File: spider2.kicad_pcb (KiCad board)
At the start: 2 copper layers, 137 x 72.5 mm, 120 parts, among them J1 NRJ6HH, J10 PJ-320A, J11 PJ359, J12 PJ359, J13 PJ359, J14 PJ359, J15 PJ359, J16 PJ359, J19 PJ359, J2 NRJ6HH, J20 PJ359, J3 PJ359, J4 PJ359, J5 PJ359, J6 PJ-320A, J7 PJ359, J8 PJ359, J9 PJ359, P1 USB4085, Q1 AOI4286, Q2 BC547, Q3 BC547, SW2 200MDP1T2B2M2QE, SW3 200MDP1T2B2M2QE, SW4 200MDP3T1B1M6QE, U2 LM7805_TO220, U4 LM4562, U5 MAX4062, U6 MAX4062, U7 PAM8406D

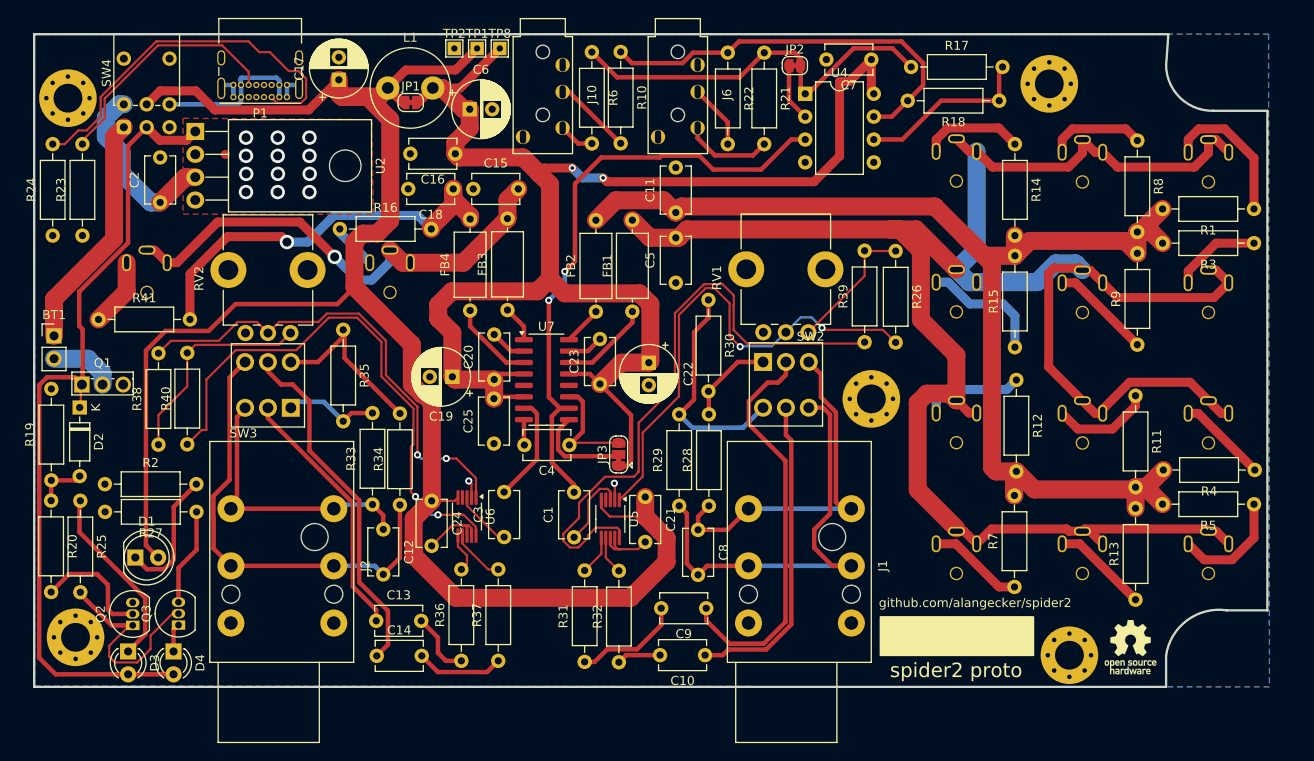
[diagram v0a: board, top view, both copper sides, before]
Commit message: 3.3V step down, fixed wrong CMV on balanced out, additional SMD footprints
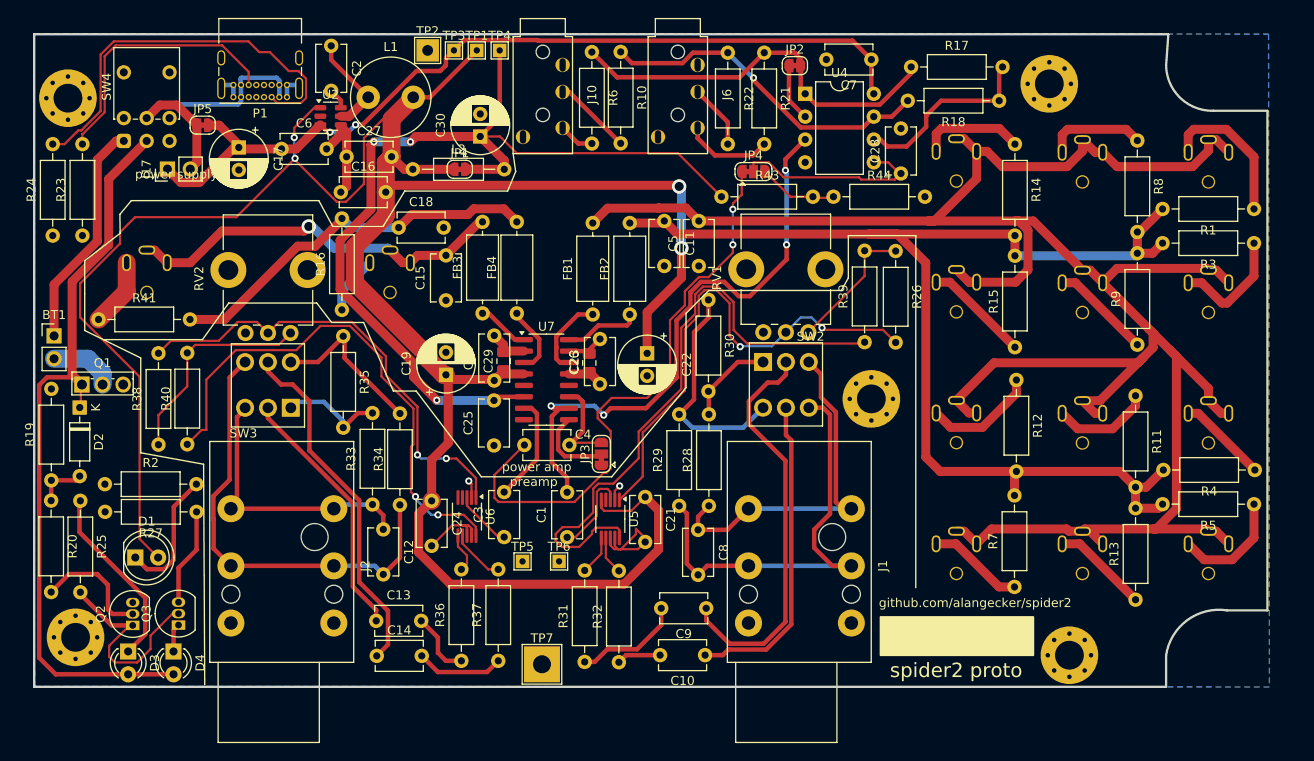
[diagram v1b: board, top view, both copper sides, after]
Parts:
- removed the REF** at (259.4, 98.7)
- removed TP8: 5VA, TestPoint:TestPoint_THTPad_1.5x1.5mm_Drill0.7mm
- added C26: alt, Capacitor_SMD:C_0805_2012Metric_Pad1.18x1.45mm_HandSolder, F.Cu at (199.3, 67.1)
- added C27: 22u, Capacitor_THT:C_Disc_D5.1mm_W3.2mm_P5.00mm, F.Cu at (172.3, 44.2)
- added C28: 100n, Capacitor_THT:C_Disc_D5.1mm_W3.2mm_P5.00mm, F.Cu at (233.9, 46.1)
- added C29: alt, Capacitor_SMD:C_0805_2012Metric_Pad1.18x1.45mm_HandSolder, F.Cu at (189.8, 66.9)
- added C30: NC, Capacitor_THT:CP_Radial_D6.3mm_P2.50mm, F.Cu at (187.2, 41.9)
- added J17: A, Connector_PinHeader_2.54mm:PinHeader_1x02_P2.54mm_Vertical, F.Cu at (152.4, 45.6)
- added JP4: SolderJumper_3_Bridged12, Jumper:SolderJumper-3_P1.3mm_Bridged12_RoundedPad1.0x1.5mm, F.Cu at (217.6, 45.8)
- added JP5: Jumper_2_Bridged, Jumper:SolderJumper-2_P1.3mm_Bridged_RoundedPad1.0x1.5mm, F.Cu at (156.4, 40.7)
- added L2: NC, Inductor_THT:L_Axial_L5.3mm_D2.2mm_P10.16mm_Horizontal_Vishay_IM-1, F.Cu at (179.7, 45.6)
- added R43: NC, Resistor_THT:R_Axial_DIN0207_L6.3mm_D2.5mm_P10.16mm_Horizontal, F.Cu at (214.0, 48.6)
- added R44: NC, Resistor_THT:R_Axial_DIN0207_L6.3mm_D2.5mm_P10.16mm_Horizontal, F.Cu at (226.4, 48.6)
- added TP3: V_in, TestPoint:TestPoint_THTPad_1.5x1.5mm_Drill0.7mm, F.Cu at (184.3, 32.4)
- added TP4: 3.3VA, TestPoint:TestPoint_THTPad_1.5x1.5mm_Drill0.7mm, F.Cu at (189.4, 32.4)
- added TP5: Floor, TestPoint:TestPoint_THTPad_1.5x1.5mm_Drill0.7mm, F.Cu at (191.9, 89.2)
- added TP6: Int., TestPoint:TestPoint_THTPad_1.5x1.5mm_Drill0.7mm, F.Cu at (196.0, 89.2)
- added TP7: GND, TestPoint:TestPoint_THTPad_4.0x4.0mm_Drill2.0mm, F.Cu at (194.1, 100.6)
- C1, C3: value 22u -> 470n
- C10, C13, C14, C9: value 22u -> 100n
- C6: value NC -> 22u; footprint Capacitor_THT:CP_Radial_D6.3mm_P2.50mm -> Capacitor_THT:C_Disc_D5.1mm_W3.2mm_P5.00mm
- C7: value NC -> 100n
- L1: value NC -> 4.7uH, >2A, <100mOhm
- R17, R18: value 10k -> 1k
- TP1: value 5V -> 3.3V
- TP2: footprint TestPoint:TestPoint_THTPad_1.5x1.5mm_Drill0.7mm -> TestPoint:TestPoint_THTPad_2.5x2.5mm_Drill1.2mm
- U2: value LM7805_TO220 -> AP63203WU; footprint Package_TO_SOT_THT:TO-220-4_Horizontal_TabDown -> Package_TO_SOT_SMD:TSOT-23-6
- U4: value LM4562 -> NE5532
- moved C2 25.8 mm to (170.6, 31.9), turned to -90 degrees
- moved C6 21.4 mm to (165.1, 43.3)
- moved U2 15.1 mm to (170.6, 39.7), turned to 0 degrees
- moved C16 13.4 mm to (171.7, 48.1), turned to 0 degrees
- moved C17 13.4 mm to (160.4, 43.2), turned to -90 degrees
- moved C15 12.7 mm to (183.4, 60.2), turned to 90 degrees
- moved JP1 9.21 mm to (184.9, 45.6)
- moved R16 8.99 mm to (171.8, 61.2), turned to 90 degrees
- moved C18 7.43 mm to (178.1, 52.1), turned to 0 degrees
- moved FB4 5.20 mm to (191.3, 61.6)
- moved FB1 4.42 mm to (199.7, 61.7)
- moved FB2 3.77 mm to (203.8, 61.7)
- moved C5 3.16 mm to (211.5, 56.3)
- moved TP2 2.97 mm to (181.4, 32.4)
- moved FB3 2.80 mm to (187.5, 61.6)
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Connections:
- net Net-(U7-VREF) renamed VREF
- C16 pad 1: +5VA -> GND
- C16 pad 2: GND -> +3.3V
- C17 pad 1: +5V -> VCC
- C19 pad 1: +5VA -> +3.3V
- C2 pad 1: Net-(SW4B-A) -> Net-(U2-SW)
- C2 pad 2: GND -> Net-(U2-BST)
- C20 pad 1: +5VA -> +3.3V
- C21 pad 1: +5V -> +3.3V
- C22 pad 1: +5VA -> +3.3V
- C23 pad 1: +5VA -> +3.3V
- C24 pad 1: +5V -> +3.3V
- C25 pad 2: +5VA -> +3.3VA
- C6 pad 1: +5VA -> VCC
- C7 pad 1: +5VA -> VCC
- D1 pad 2: +5V -> +3.3V
- D2 pad 1: V_BAT -> +BATT
- D3 pad 2: V_BAT -> +BATT
- D4 pad 2: V_BAT -> +BATT
- JP1 pad 1: +5V -> +3.3V
- JP1 pad 2: +5VA -> +3.3VA
- JP3 pad 1: +5VA -> +3.3V
- L1 pad 1: +5V -> Net-(U2-SW)
- L1 pad 2: +5VA -> +3.3V
- Q1 pad 1: V_BAT -> +BATT
- SW4 pad 2: V_BAT -> +BATT
- SW4 pad 4: Net-(SW4B-A) -> +BATT
- SW4 pad 5: +5V -> Net-(J17-Pin_2)
- TP1 pad 1: +5V -> +3.3V
- U2 pad 1: V_BAT -> +3.3V
- U2 pad 2: GND -> VCC
- U2 pad 3: Net-(SW4B-A) -> VCC
- U2 pad 4: (no net) -> GND
- U4 pad 5: GND -> Net-(JP4-C)
- U4 pad 8: +5VA -> VCC
- U5 pad 5: +5V -> +3.3V
- U6 pad 5: +5V -> +3.3V
- U7 pad 13: +5VA -> +3.3V
- U7 pad 4: +5VA -> +3.3V
- U7 pad 6: +5VA -> +3.3VA
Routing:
- net +3.3V: track 0.00 -> 276.4 mm, vias 0 -> 4
- net +5V: track 206.8 -> 0.00 mm
- net +5VA: track 174.0 -> 0.00 mm, vias 2 -> 0
- net +3.3VA: track 0.00 -> 105.7 mm, vias 0 -> 3
- net VCC: track 0.00 -> 96.0 mm, vias 0 -> 2
- net V_BAT: track 92.4 -> 0.00 mm
- net +BATT: track 0.00 -> 85.0 mm
- net VREF: track 2.84 -> 65.0 mm, vias 0 -> 2
- net Net-(JP4-C): track 0.00 -> 22.0 mm
- net Net-(SW4B-A): track 20.2 -> 0.00 mm
- net GND: track 45.1 -> 59.4 mm, vias 14 -> 2
- net Net-(J17-Pin_2): track 0.00 -> 12.2 mm
- net Net-(U2-SW): track 0.00 -> 11.3 mm
- net Net-(C15-Pad2): track 53.7 -> 43.1 mm
- net Net-(C5-Pad2): track 248.9 -> 258.1 mm
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- removed copper zone on F.Cu, net GND
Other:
- board text added: "power amp"
- board text added: "power supply"
- board text added: "preamp"

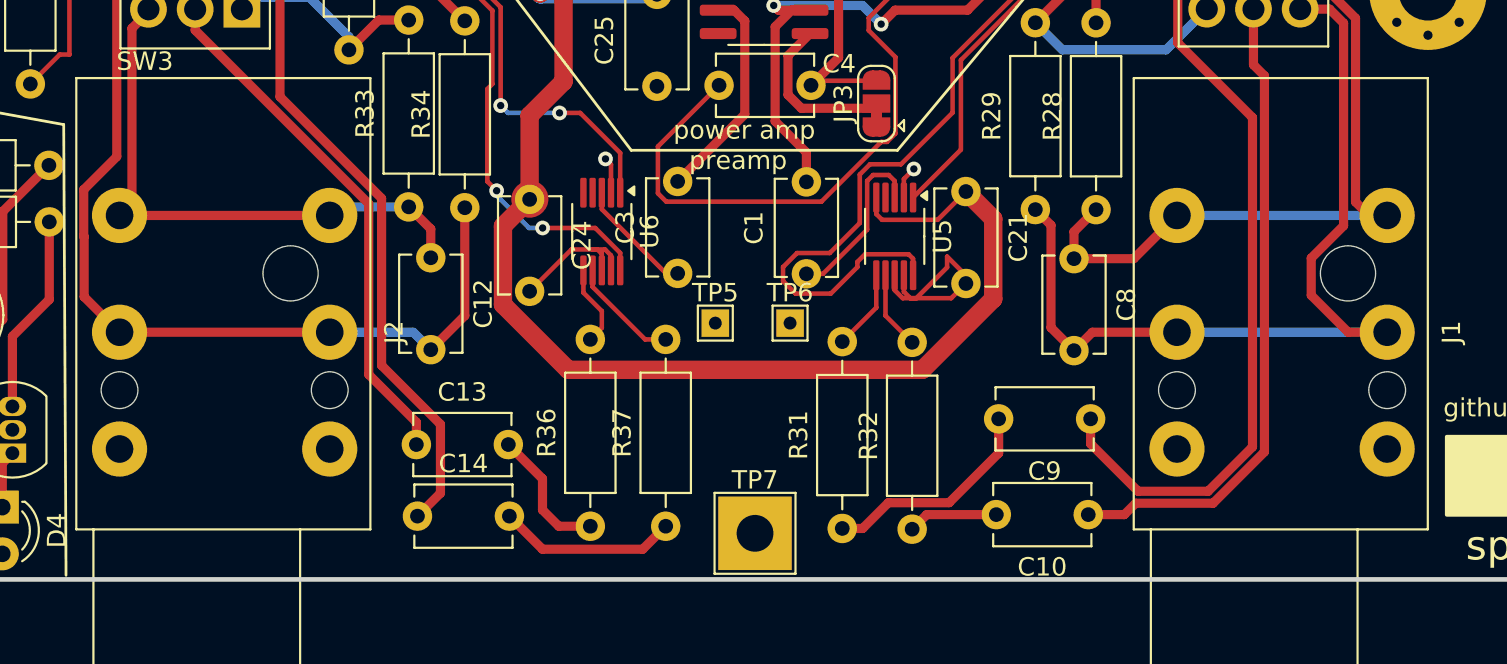
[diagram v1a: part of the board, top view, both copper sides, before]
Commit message: jumper for switching input jacks between GND and BIAS
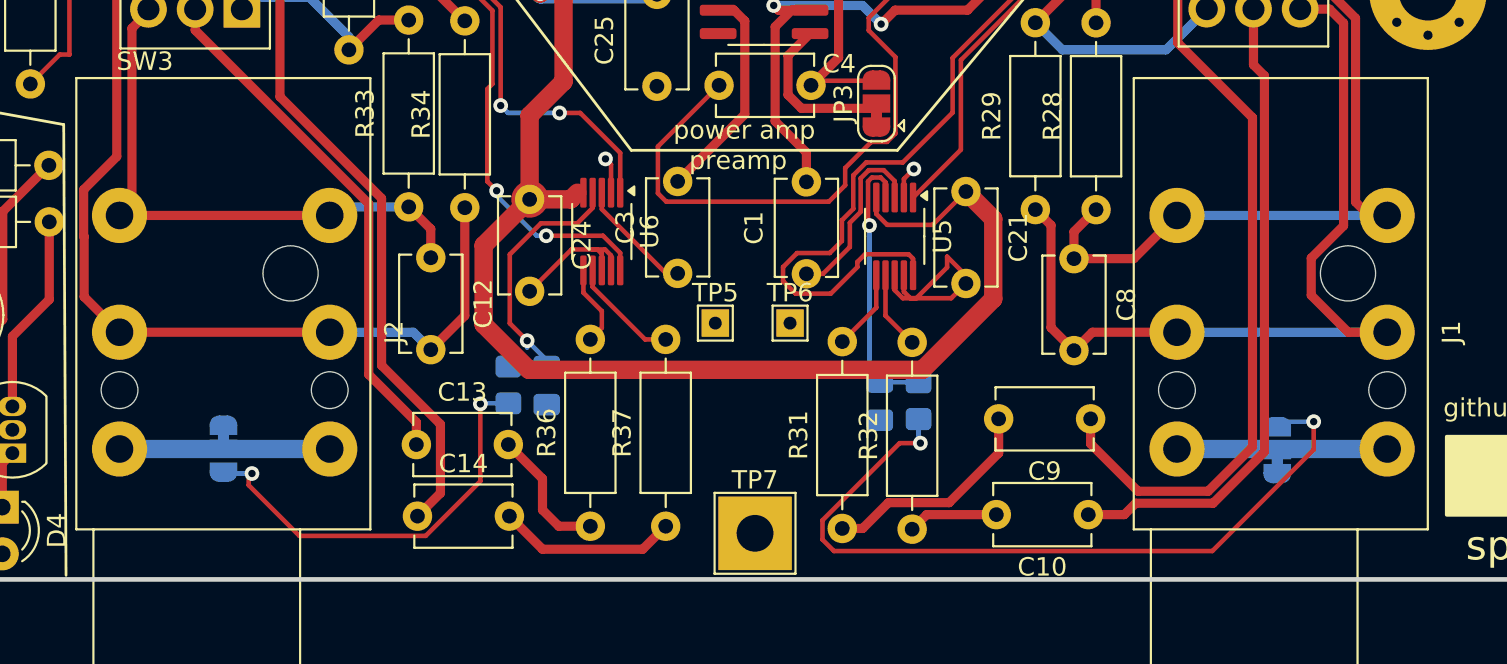
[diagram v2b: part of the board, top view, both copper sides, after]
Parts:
- added C31: NC, Capacitor_SMD:C_0805_2012Metric_Pad1.18x1.45mm_HandSolder, B.Cu at (200.8, 93.4)
- added C32: NC, Capacitor_SMD:C_0805_2012Metric_Pad1.18x1.45mm_HandSolder, B.Cu at (182.7, 92.6)
- added JP6: SolderJumper_3_Bridged12, Jumper:SolderJumper-3_P1.3mm_Bridged12_RoundedPad1.0x1.5mm, B.Cu at (222.5, 96.1)
- added JP7: SolderJumper_3_Bridged12, Jumper:SolderJumper-3_P1.3mm_Bridged12_RoundedPad1.0x1.5mm, B.Cu at (165.2, 96.0)
- added R42: NC, Resistor_SMD:R_0805_2012Metric_Pad1.20x1.40mm_HandSolder, B.Cu at (202.9, 93.4)
- added R45: NC, Resistor_SMD:R_0805_2012Metric_Pad1.20x1.40mm_HandSolder, B.Cu at (180.6, 92.5)
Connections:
- J1 pad S: GND -> Net-(JP6-C)
- J1 pad SN: GND -> Net-(JP6-C)
- J2 pad S: GND -> Net-(JP7-C)
- J2 pad SN: GND -> Net-(JP7-C)
- U5 pad 4: unconnected-(U5-BIAS-Pad4) -> Net-(U5-BIAS)
- U6 pad 4: unconnected-(U6-BIAS-Pad4) -> Net-(U6-BIAS)
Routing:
- net /Preamp Interpreter/BIAS: track 0.00 -> 42.3 mm, vias 0 -> 2
- net /Preamp Floor/BIAS: track 0.00 -> 23.0 mm, vias 0 -> 2
- net Net-(U6-BIAS): track 0.00 -> 15.8 mm, vias 0 -> 1
- net Net-(U5-BIAS): track 0.00 -> 15.3 mm, vias 0 -> 1
- net Net-(JP7-C): track 0.00 -> 11.4 mm
- net Net-(JP6-C): track 0.00 -> 11.4 mm
- net +3.3V: track 276.4 -> 281.5 mm
- net VREF: track 65.0 -> 65.6 mm
- net /Preamp Interpreter/OUT: track 9.61 -> 10.1 mm

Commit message: specify parts and load simulation R
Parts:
- added R46: NC, Resistor_THT:R_Axial_Power_L25.0mm_W9.0mm_P7.62mm_Vertical, F.Cu at (273.2, 66.2)
- FB1, FB2, FB3, FB4: value FerriteBead_Small -> 3A, >100 Ohm@100MHz
- moved C18 5.57 mm to (183.2, 49.7), turned to -90 degrees
- moved C22 2.77 mm to (205.8, 68.8), turned to 90 degrees
- moved C15 1.75 mm to (183.3, 61.9)
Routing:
- net Net-(C11-Pad1): track 135.1 -> 156.9 mm
- net +3.3V: track 281.5 -> 292.8 mm
- net Net-(C15-Pad2): track 43.1 -> 44.8 mm
- net Net-(C18-Pad1): track 42.9 -> 43.7 mm

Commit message: credits on PCB
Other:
- board text added: "COATI Alis Spider chandi Matthias"
- board text added: "originally developed by inspired by new board by with great help of built by"
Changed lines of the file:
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@@
 		)
+	)
+	(gr_rect
+		(start 224.2566 101.0158)
+		(end 236.9693 98.5266)
+		(stroke
+			(width 0.15)
+			(type solid)
+		)
+		(fill solid)
+		(layer "B.SilkS")
 	)
 	(gr_line
@@
 		(layer "Edge.Cuts")
 	)
+	(gr_text "COATI\nAlis Spider\nchandi\nMatthias\n"
+		(at 236.8804 97.9932 -0)
+		(layer "B.SilkS")
+		(effects
+			(font
+				(size 1 1)
+				(thickness 0.2)
+				(bold yes)
+			)
+			(justify left bottom mirror)
+		)
+	)
+	(gr_text "originally developed by\ninspired by\nnew board by\nwith great help of\nbuilt by\n"
+		(at 237.3122 99.5934 0)
+		(layer "B.SilkS")
+		(effects
+			(font
+				(size 1 0.9)
+				(thickness 0.15)
+			)
+			(justify right bottom mirror)
+		)
+	)
 	(gr_text "github.com/alangecker/spider2"

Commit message: minor credits change
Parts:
- moved R7 0.76 mm to (247.2, 91.6)
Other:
- board text added: "COATI Alis Spider chandi Matthias<3"
- board text removed: "COATI Alis Spider chandi Matthias"
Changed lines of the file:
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@@
 	(footprint "Resistor_THT:R_Axial_DIN0207_L6.3mm_D2.5mm_P10.16mm_Horizontal"
 		(layer "F.Cu")
-		(at 246.55 91.99 90)
+		(at 247.1928 91.5924 90)
 		(descr "Resistor, Axial_DIN0207 series, Axial, Horizontal, pin pitch=10.16mm, 0.25W = 1/4W, length*diameter=6.3*2.5mm^2, http://cdn-reichelt.de/documents/datenblatt/B400/1_4W%23YAG.pdf")
 		(tags "Resistor Axial_DIN0207 series Axial Horizontal pin pitch 10.16mm 0.25W = 1/4W length 6.3mm diameter 2.5mm")
@@
 	)
 	(gr_rect
-		(start 224.2566 101.0158)
-		(end 236.9693 98.5266)
+		(start 224.8154 101.5238)
+		(end 237.5281 99.0346)
 		(stroke
 			(width 0.15)
@@
 		(layer "Edge.Cuts")
 	)
-	(gr_text "COATI\nAlis Spider\nchandi\nMatthias\n"
-		(at 236.8804 97.9932 -0)
+	(gr_text "COATI\nAlis Spider\nchandi\nMatthias<3\n"
+		(at 237.4392 98.5012 0)
 		(layer "B.SilkS")
 		(effects
 			(font
-				(size 1 1)
+				(size 1 0.95)
 				(thickness 0.2)
 				(bold yes)
@@
 	)
 	(gr_text "originally developed by\ninspired by\nnew board by\nwith great help of\nbuilt by\n"
-		(at 237.3122 99.5934 0)
+		(at 237.871 100.1014 0)
 		(layer "B.SilkS")
 		(effects
 			(font
-				(size 1 0.9)
+				(size 1 0.85)
 				(thickness 0.15)
 			)
@@
 	)
 	(segment
-		(start 240.04 87.2)
-		(end 237.849112 87.2)
+		(start 247.1928 91.5924)
+		(end 244.4324 91.5924)
 		(width 1)
 		(layer "F.Cu")
@@
 	)
 	(segment
-		(start 246.55 91.99)
-		(end 244.83 91.99)
+		(start 240.04 87.2)
+		(end 237.849112 87.2)
 		(width 1)
 		(layer "F.Cu")
@@
 	)
 	(segment
-		(start 244.83 91.99)
+		(start 244.4324 91.5924)
 		(end 240.04 87.2)
 		(width 1)
@@
 	)
 	(segment
+		(start 246.76 80.9996)
+		(end 246.76 79.16)
+		(width 1)
+		(layer "F.Cu")
+		(net 16)
+	)
+	(segment
 		(start 260.2 52.56)
 		(end 260.44 52.56)
@@
 	)
 	(segment
+		(start 247.1928 81.4324)
+		(end 246.76 80.9996)
+		(width 1)
+		(layer "F.Cu")
+		(net 16)
+	)
+	(segment
 		(start 233.51281 52.7872)
 		(end 236.7 55.97439)
@@
 	)
 	(segment
-		(start 246.55 81.83)
-		(end 246.55 79.37)
-		(width 1)
-		(layer "F.Cu")
-		(net 16)
-	)
-	(segment
 		(start 246.4272 52.7872)
 		(end 246.6 52.96)
@@
 		(width 1)
 		(layer "F.Cu")
-		(net 16)
-	)
-	(segment
-		(start 246.55 79.37)
-		(end 246.76 79.16)
-		(width 1)
-		(layer "F.Cu")
